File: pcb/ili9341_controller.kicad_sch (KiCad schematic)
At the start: 42 parts, among them J1 USB_B_Micro, U1 ICE40UP5K-SG48ITR, U2 LM3880, U3 LD1117S33TR_SOT223, U4 LD1117S12TR_SOT223, U5 LD1117S25TR_SOT223, U6 RP2040

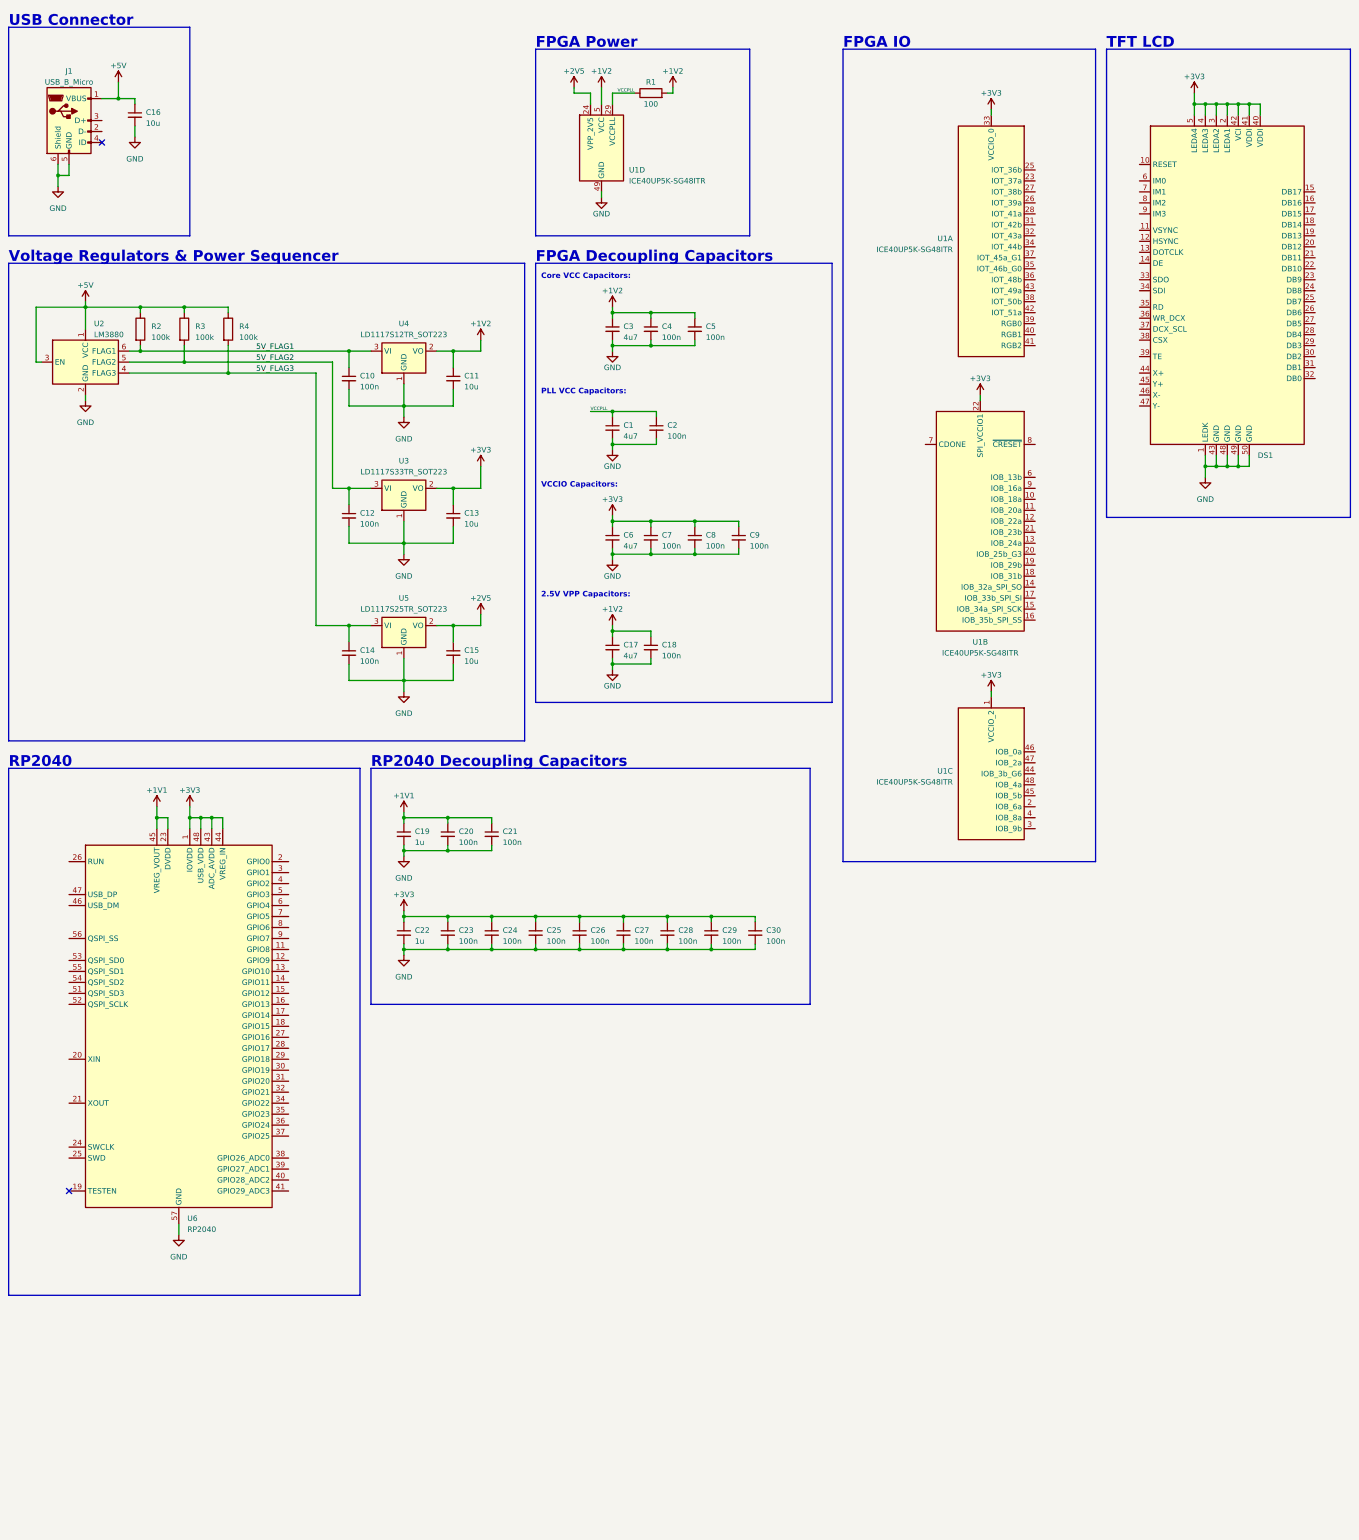
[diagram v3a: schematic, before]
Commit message: add rp2040 reset/boot switches; set up flash memory; add usb connection to rp2040
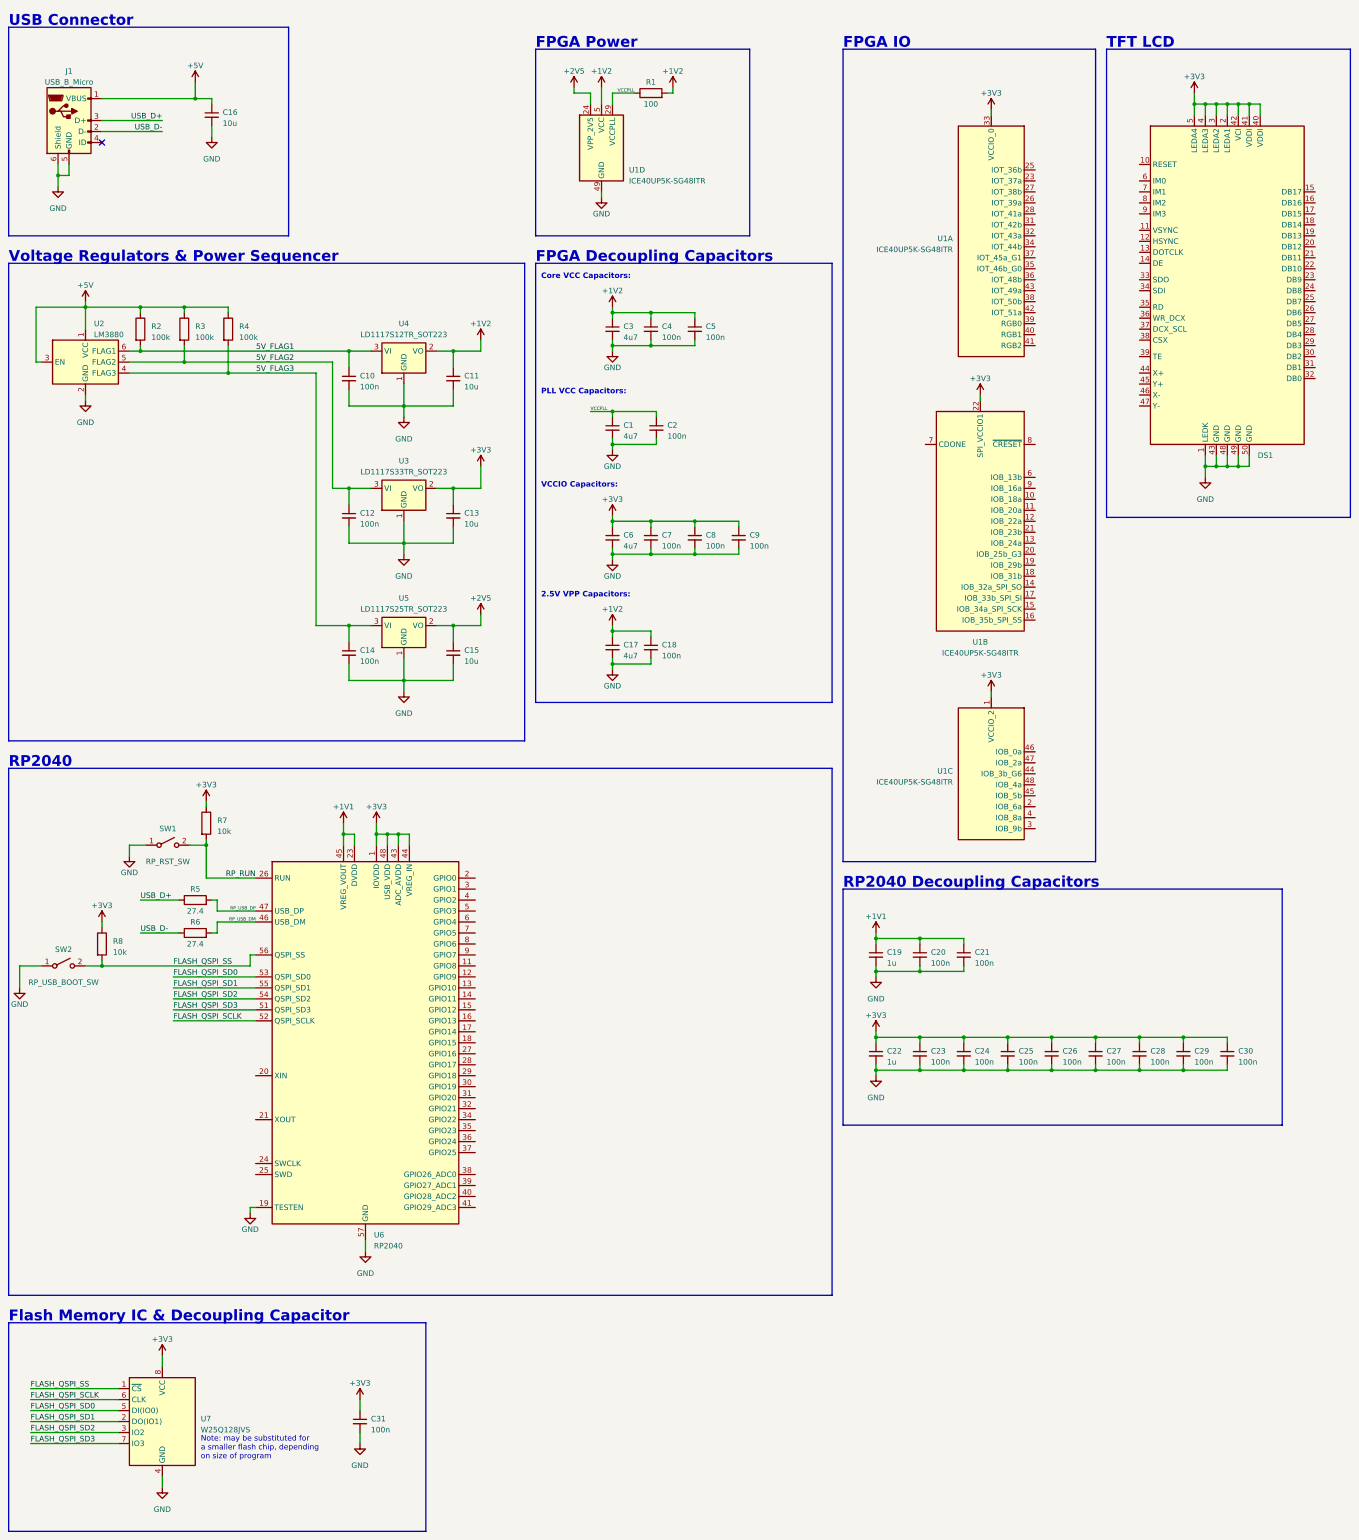
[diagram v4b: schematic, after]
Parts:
- added C31: 100n, symbol Device:C_Small
- added R5, R6: 27.4, symbol Device:R
- added R7, R8: 10k, symbol Device:R
- added SW1: RP_RST_SW, symbol Switch:SW_SPST
- added SW2: RP_USB_BOOT_SW, symbol Switch:SW_SPST
- added U7: W25Q128JVS, Package_SO:SOIC-8_5.23x5.23mm_P1.27mm, symbol Memory_Flash:W25Q128JVS
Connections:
- net +3V3: now also C31.1, R7.1, R8.1, U7.8 (VCC)
- net GND: now also U6.19 (TESTEN), C31.2, SW1.1 (A), SW2.1 (A), U7.4 (GND)
- net USB_D-: now reaches J1.2 (D-)
- net USB_D-: now also R6.1
- net USB_D+: now reaches J1.3 (D+)
- net USB_D+: now also R5.1
- net RP_RUN: now reaches U6.26 (RUN)
- net RP_RUN: now also R7.2, SW1.2 (B)
- net RP_USB_DM: now reaches U6.46 (USB_DM)
- net RP_USB_DM: now also R6.2
- net RP_USB_DP: now reaches U6.47 (USB_DP)
- net RP_USB_DP: now also R5.2
- net FLASH_QSPI_SD3: now reaches U6.51 (QSPI_SD3)
- net FLASH_QSPI_SD3: now also U7.7 (IO3)
- net FLASH_QSPI_SCLK: now reaches U6.52 (QSPI_SCLK)
- net FLASH_QSPI_SCLK: now also U7.6 (CLK)
- net FLASH_QSPI_SD0: now reaches U6.53 (QSPI_SD0)
- net FLASH_QSPI_SD0: now also U7.5 (DI(IO0))
- net FLASH_QSPI_SD2: now reaches U6.54 (QSPI_SD2)
- net FLASH_QSPI_SD2: now also U7.3 (IO2)
- net FLASH_QSPI_SD1: now reaches U6.55 (QSPI_SD1)
- net FLASH_QSPI_SD1: now also U7.2 (DO(IO1))
- net FLASH_QSPI_SS: now reaches U6.56 (QSPI_SS)
- net FLASH_QSPI_SS: now also R8.2, SW2.2 (B), U7.1 (~{CS})
- no-connect marks 2 -> 1
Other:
- note added: "Flash Memory IC & Decoupling Capacitor"
- note added: "Note: may be substituted for a smaller flash chip, depending on size of program"
- moved on the sheet: C16, C19, C20, C21, C22, C23, C24, C25, C26, C27, C28, C29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

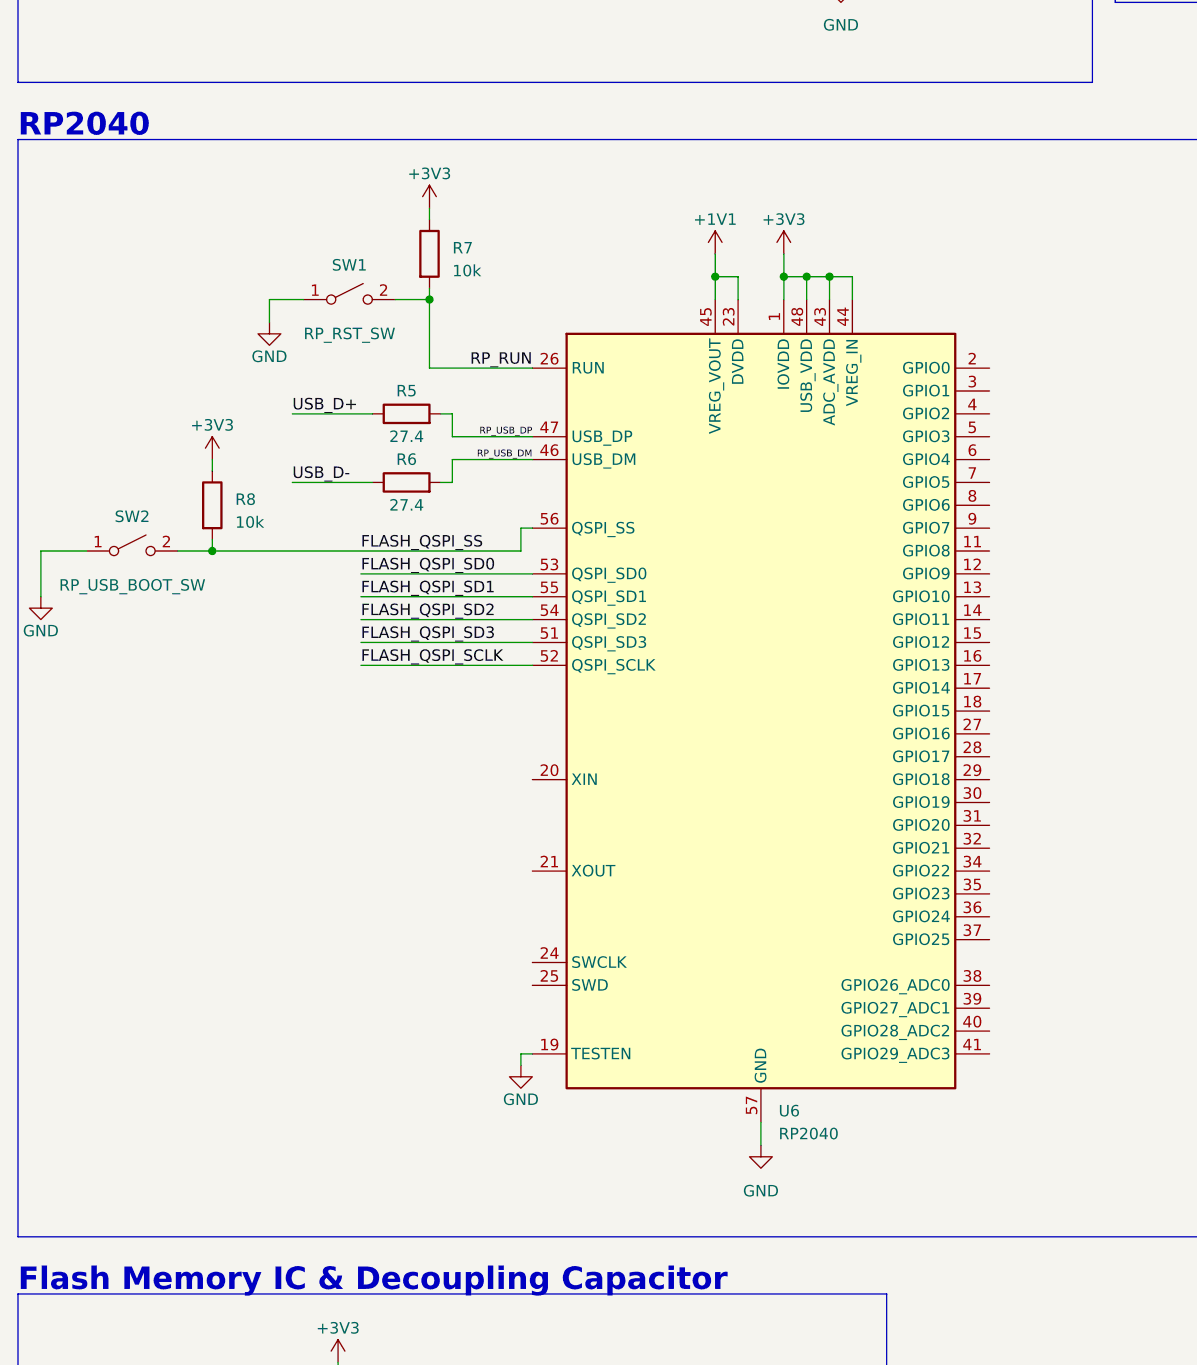
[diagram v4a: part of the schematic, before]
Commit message: finish connections to rp2040 (besides gpios)
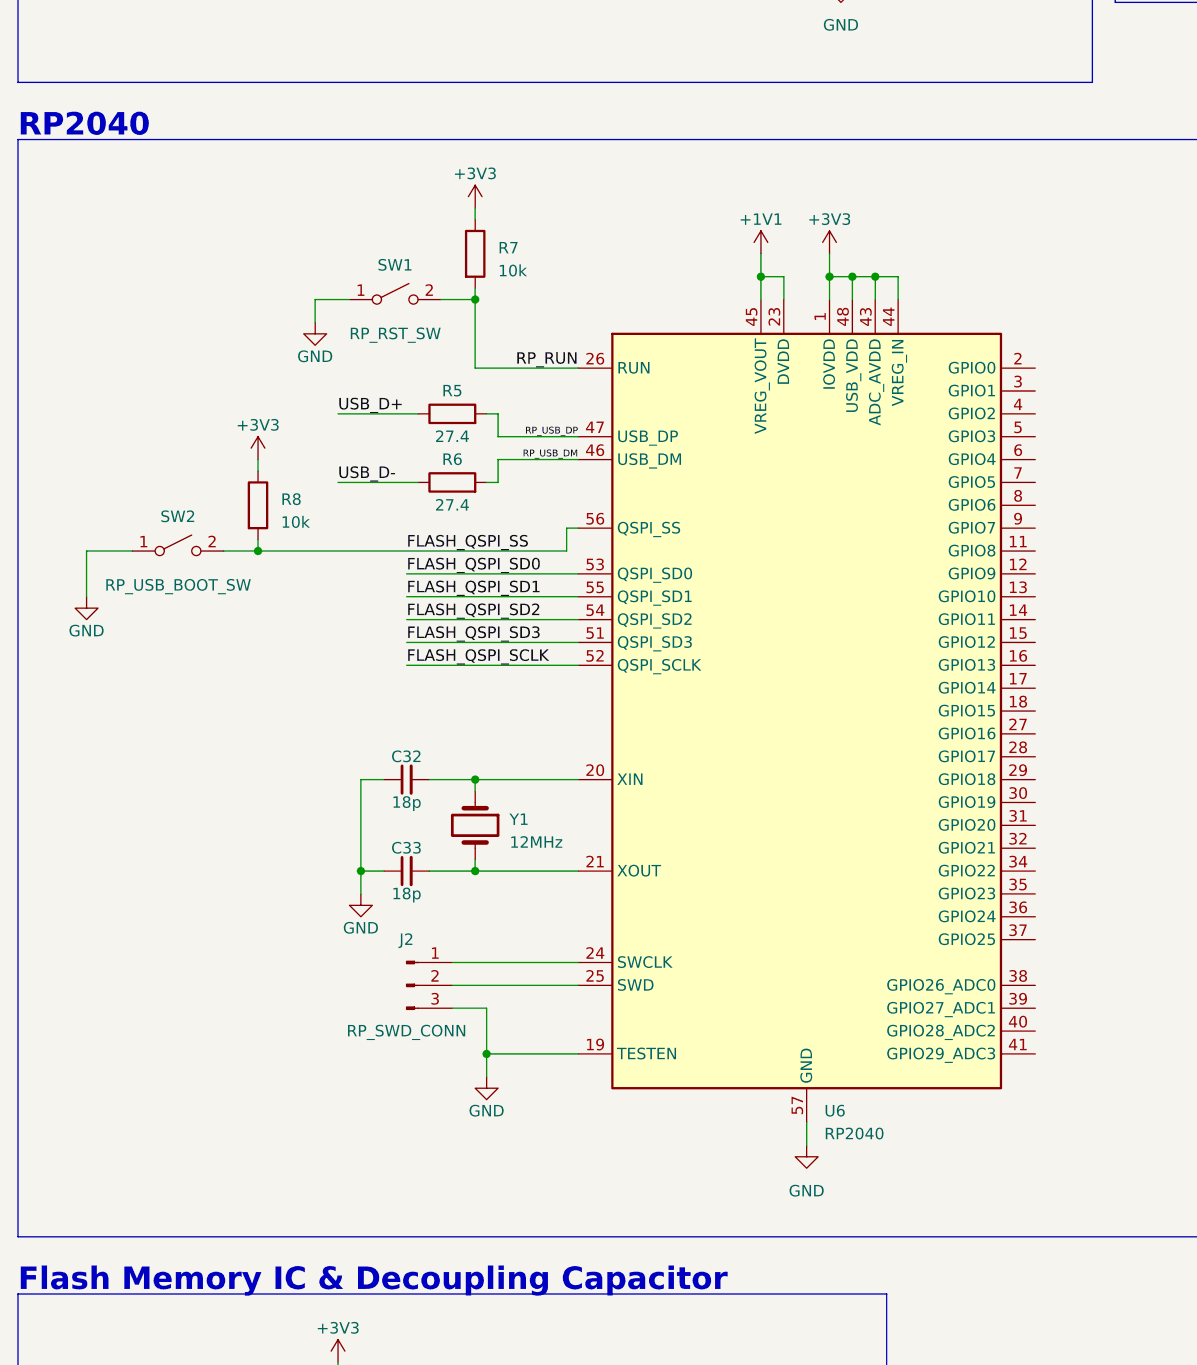
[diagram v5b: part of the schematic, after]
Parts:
- added C32, C33: 18p, symbol Device:C_Small
- added J2: RP_SWD_CONN, symbol Connector:Conn_01x03_Pin
- added Y1: 12MHz, symbol Device:Crystal
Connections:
- net GND: now also C32.1, C33.1, J2.3 (Pin_3)
- net at U6.20 (XIN): now also C32.2, Y1.1
- net at U6.21 (XOUT): now also C33.2, Y1.2
- net at U6.24 (SWCLK): now also J2.1 (Pin_1)
- net at U6.25 (SWD): now also J2.2 (Pin_2)
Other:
- moved on the sheet: R5, R6, R7, R8, SW1, SW2, U6

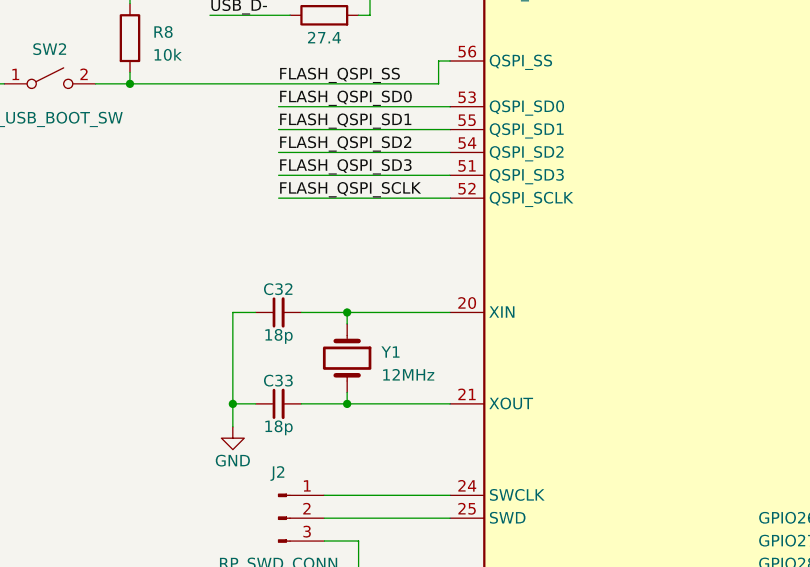
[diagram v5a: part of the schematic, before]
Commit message: clarify crystal oscillator model
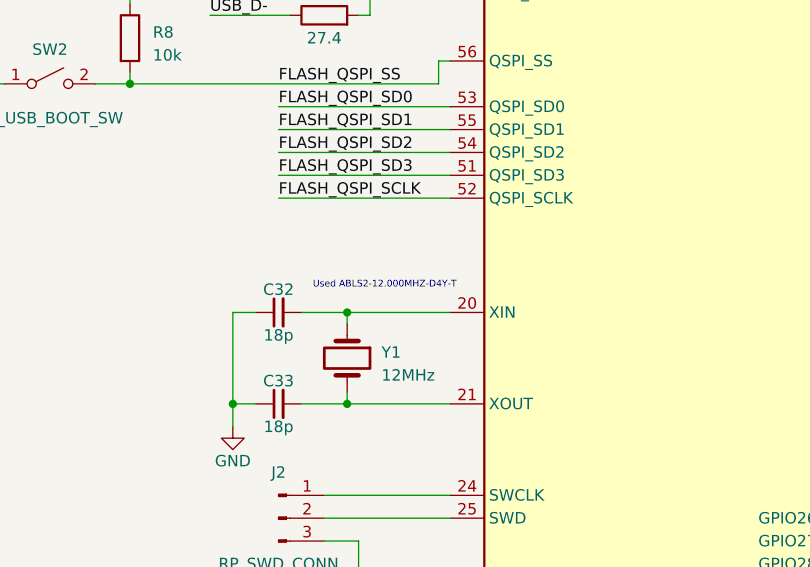
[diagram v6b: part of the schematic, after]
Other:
- note added: "Used ABLS2-12.000MHZ-D4Y-T"
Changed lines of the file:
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@@
     (effects (font (size 2.5 2.5) (thickness 0.5) bold) (justify left bottom))
+  )
+  (text "Used ABLS2-12.000MHZ-D4Y-T" (at 72.39 265.43 0)
+    (effects (font (size 0.75 0.75)) (justify left bottom))
   )
   (text "PLL VCC Capacitors:" (at 148.59 110.49 0)

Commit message: add labels to TFT LCD in pcb
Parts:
- added R10, R9: 10k, symbol Device:R
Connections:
- net +3V3: now also DS1.7 (IM1), DS1.8 (IM2), R10.1, R9.1
- net GND: now also DS1.6 (IM0), DS1.9 (IM3)
- net FPGA_CDONE: now reaches U1.7 (CDONE)
- net FPGA_CDONE: now also R9.2
- net FPGA_CRESET: now reaches U1.8 (~{CRESET})
- net FPGA_CRESET: now also R10.2
- net TFT_CS: now reaches U6.2 (GPIO0)
- net TFT_CS: now also DS1.38 (CSX)
- net TFT_DCX: now reaches U6.3 (GPIO1)
- net TFT_DCX: now also DS1.36 (WR_DCX)
- net TFT_SCL: now reaches U6.4 (GPIO2)
- net TFT_SCL: now also DS1.37 (DCX_SCL)
- net TFT_SDI: now reaches U6.5 (GPIO3)
- net TFT_SDI: now also DS1.34 (SDI)
- net TFT_RESET: now reaches U6.6 (GPIO4)
- net TFT_RESET: now also DS1.10 (RESET)
- net TFT_VSYNC: now reaches DS1.11 (VSYNC)
- net TFT_HSYNC: now reaches DS1.12 (HSYNC)
- net TFT_DOTCLK: now reaches DS1.13 (DOTCLK)
- net TFT_DE: now reaches DS1.14 (DE)
- net TFT_DATA_RED4: now reaches DS1.15 (DB17)
- net TFT_DATA_RED3: now reaches DS1.16 (DB16)
- net TFT_DATA_RED2: now reaches DS1.17 (DB15)
- net TFT_DATA_RED1: now reaches DS1.18 (DB14)
- net TFT_DATA_RED0: now reaches DS1.19 (DB13)
- net TFT_DATA_GREEN5: now reaches DS1.21 (DB11)
- net TFT_DATA_GREEN4: now reaches DS1.22 (DB10)
- net TFT_DATA_GREEN3: now reaches DS1.23 (DB9)
- net TFT_DATA_GREEN2: now reaches DS1.24 (DB8)
- net TFT_DATA_GREEN1: now reaches DS1.25 (DB7)
- net TFT_DATA_GREEN0: now reaches DS1.26 (DB6)
- net TFT_DATA_BLUE4: now reaches DS1.27 (DB5)
- net TFT_DATA_BLUE3: now reaches DS1.28 (DB4)
- net TFT_DATA_BLUE2: now reaches DS1.29 (DB3)
- net TFT_DATA_BLUE1: now reaches DS1.30 (DB2)
- net TFT_DATA_BLUE0: now reaches DS1.31 (DB1)
- no-connect marks 1 -> 10
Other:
- note added: "IM[3:0] = 0110 meaning 4-wire SPI see pg. 26 of ILI9341 datasheet"
- note added: "see pg. 45 of ILI9341 datasheet for 16-bit pin layout"
- moved on the sheet: DS1, U1B
